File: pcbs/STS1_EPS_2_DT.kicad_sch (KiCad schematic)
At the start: 19 parts, among them Q2 SI7272DP-T1-GE3, Q3 2N7002, U1 4072, U2 LTC6995IDCB-1

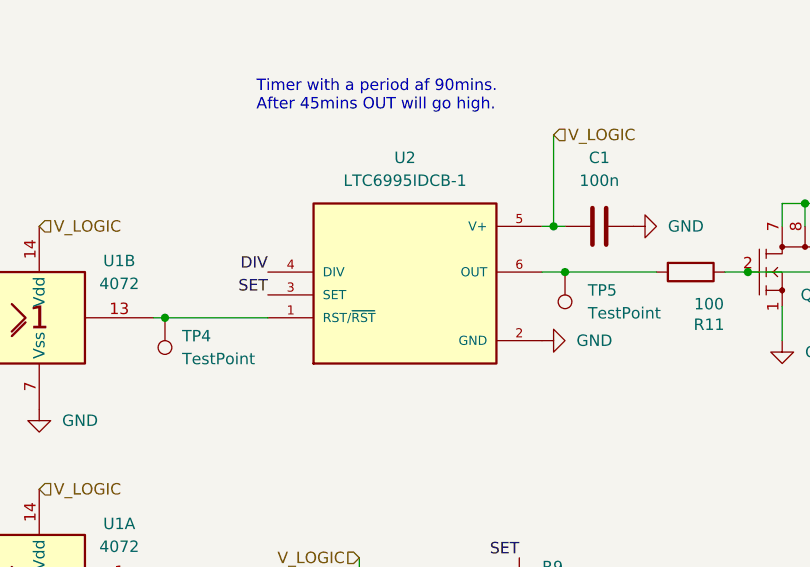
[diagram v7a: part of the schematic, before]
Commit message: Fixed deployment timer symbol having wrong pin numbers.
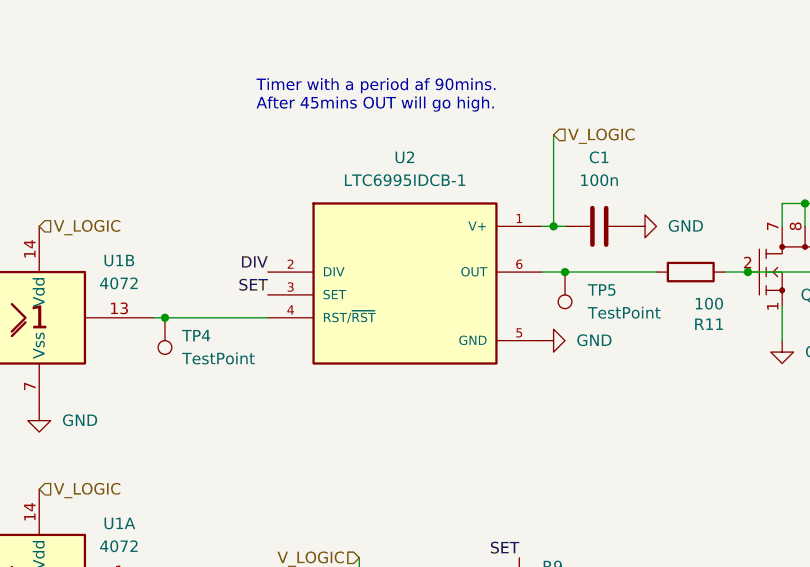
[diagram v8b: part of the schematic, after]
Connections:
- net DIV: now also U2.2 (DIV); no longer U2.4 (DIV)
- net GND: now also U2.5 (GND), U2.7 (GND); no longer U2.2 (GND)
- net V_LOGIC: now also U2.1 (V+); no longer U2.5 (V+)
- net at TP4.1, U1.13: now also U2.4 (RST/~{RST}); no longer U2.1 (RST/~{RST})
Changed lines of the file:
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@@
 		)
 		(property "Footprint" "Package_DFN_QFN:DFN-6-1EP_3x2mm_P0.5mm_EP1.65x1.35mm"
-			(at 133.35 90.17 0)
+			(at 106.426 79.248 0)
 			(effects
 				(font
@@
 		)
 		(property "STANDARD" "IPC 7351B"
-			(at 133.35 90.17 0)
+			(at 113.538 73.914 0)
 			(effects
 				(font
@@
 		)
 		(property "MAXIMUM_PACKAGE_HEIGHT" "1.0mm"
-			(at 133.35 90.17 0)
+			(at 130.302 74.168 0)
 			(effects
 				(font
@@
 		)
 		(property "MANUFACTURER" "Analog Devices Inc."
-			(at 133.35 90.17 0)
+			(at 125.222 77.216 0)
 			(effects
 				(font
@@
 		)
 		(property "PARTREV" "Rev. B"
-			(at 133.35 90.17 0)
+			(at 128.524 72.644 0)
 			(effects
 				(font
@@
 		(pin "6"
 		)
+		(pin "7"
+		)
 		(instances
